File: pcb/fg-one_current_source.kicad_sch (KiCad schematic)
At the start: 23 parts, among them Q1 BC547, Q2 IRF9540N, Q3 IRF9540N, U6 LM358, U9 TL071

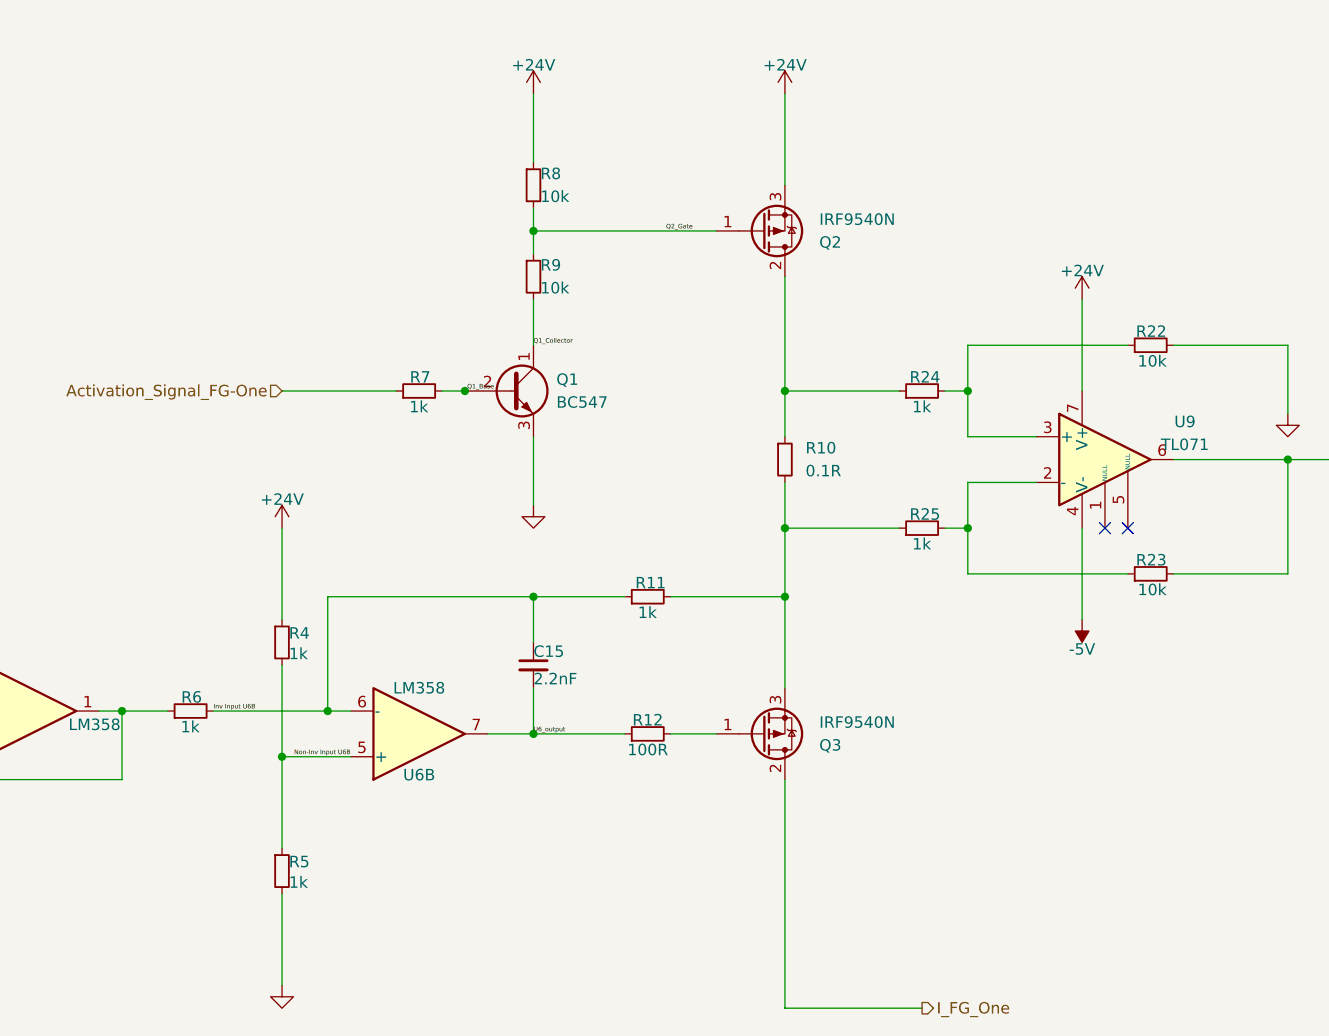
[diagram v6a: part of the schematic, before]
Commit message: sma measurement added, new connector for leds, some minor fixes
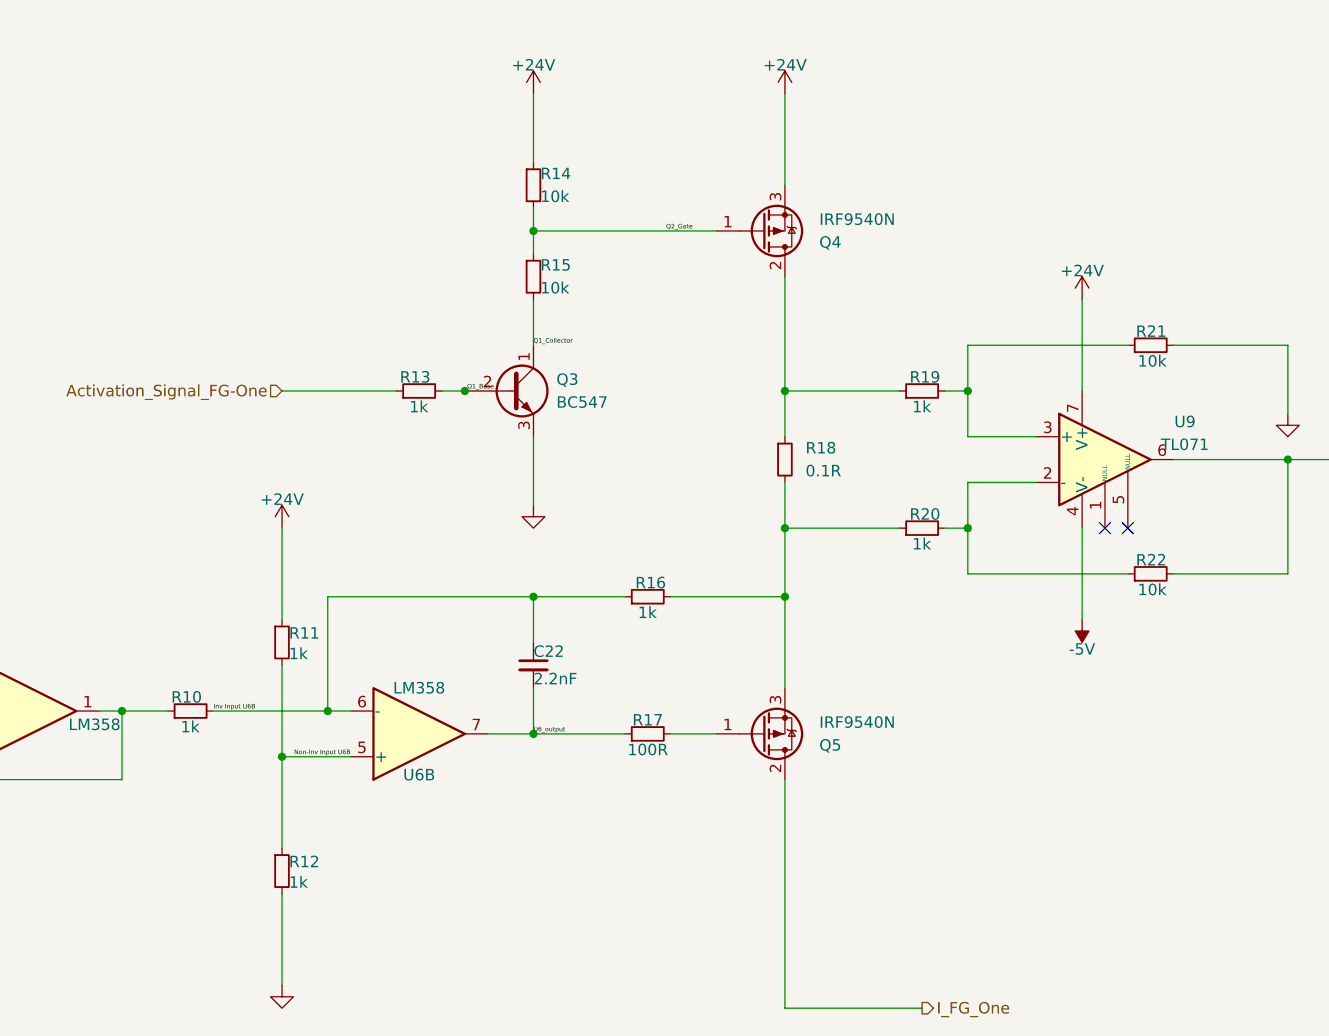
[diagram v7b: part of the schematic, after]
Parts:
- renumbered C15 to C22, Q1 to Q3, Q2 to Q4, Q3 to Q5, R6 to R10, R4 to R11, R5 to R12, R7 to R13, R8 to R14, R9 to R15, R11 to R16, R12 to R17, R10 to R18, R24 to R19, R25 to R20, R22 to R21, R23 to R22

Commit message: final version schematic?
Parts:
- added D? (x2): 1N5819, Diode_THT:D_DO-41_SOD81_P10.16mm_Horizontal, symbol Diode:1N5819
- added R66: 1k, Resistor_THT:R_Axial_DIN0207_L6.3mm_D2.5mm_P10.16mm_Horizontal, symbol Device:R_Small
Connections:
- net GND: now also D?.2 (A)
- net shunt_fg-one: now also D?.1 (K), D?.2 (A), R66.2; no longer R22.2, U9.6
- new net: R22.2, R66.1, U9.6
- new net +5V: D?.1 (K)
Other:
- company: (none) -> /dev/tal e.V.
- title: (none) -> FG-One Current Source
- moved on the sheet: C13, C14
